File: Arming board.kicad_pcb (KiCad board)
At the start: 4 copper layers, 22 parts, among them IC1 CD4043BDR, J3 Conn_01x04, Q1 SQS141ELNW-T1_GE3

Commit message: Basic routing and fixes
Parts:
- added H1: MountingHole_Pad, MountingHole:MountingHole_3.2mm_M3_DIN965_Pad_TopBottom, F.Cu at (99.5, 112.5)
- added H2: MountingHole_Pad, MountingHole:MountingHole_3.2mm_M3_DIN965_Pad_TopBottom, F.Cu at (66.5, 112.5)
- added H3: MountingHole_Pad, MountingHole:MountingHole_3.2mm_M3_DIN965_Pad_TopBottom, F.Cu at (100.0, 75.5)
- added H4: MountingHole_Pad, MountingHole:MountingHole_3.2mm_M3_DIN965_Pad_TopBottom, F.Cu at (67.0, 75.0)
- C1, C2: value 1u -> 10u
- R3, R4: value 10k -> 1k
- R6, R7: value 10k -> 80k
- moved D6 54.7 mm to (72.5, 79.4), turned to 180 degrees
- moved D19 43.5 mm to (94.6, 79.4)
- moved Q1 42.2 mm to (82.5, 80.6)
- moved J4 33.8 mm to (71.3, 99.5), turned to 90 degrees
- moved R7 31.0 mm to (83.8, 99.7)
- moved IC1 30.2 mm to (83.6, 91.8), turned to 90 degrees
- moved J2 28.0 mm to (96.0, 84.9), turned to -90 degrees
- moved R6 28.0 mm to (87.0, 99.1), turned to 180 degrees
- moved R1 27.2 mm to (79.9, 84.5), turned to 180 degrees
- moved J5 25.3 mm to (96.0, 97.6), turned to -90 degrees
- moved R2 21.7 mm to (87.0, 84.5), turned to 180 degrees
- moved C1 20.8 mm to (87.0, 101.0)
- moved C2 19.3 mm to (83.7, 101.0), turned to 180 degrees
- moved D1 18.7 mm to (84.5, 104.2), turned to 90 degrees
- moved J1 16.7 mm to (71.4, 87.5), turned to 90 degrees
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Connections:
- D5 pad 1: +BATT -> VCC
- D6 pad 1: +BATT -> VCC
- IC1 pad 11: unconnected-(IC1-R3-Pad11) -> GND
- IC1 pad 12: unconnected-(IC1-S3-Pad12) -> GND
- IC1 pad 14: unconnected-(IC1-S4-Pad14) -> GND
- IC1 pad 15: unconnected-(IC1-R4-Pad15) -> GND
- IC1 pad 3: unconnected-(IC1-R1-Pad3) -> GND
- IC1 pad 4: unconnected-(IC1-S1-Pad4) -> GND
- J1 pad 3: +BATT -> VCC
- J1 pad 4: +BATT -> VCC
- J3 pad 2: Net-(D3-K) -> Net-(D1-K)
- J3 pad 3: Net-(D1-K) -> Net-(D3-K)
- J4 pad 3: +BATT -> VCC
- J4 pad 4: +BATT -> VCC
- Q1 pad 1: +BATT -> VCC
- Q1 pad 2: +BATT -> VCC
- Q1 pad 3: +BATT -> VCC
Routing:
- net VCC: track 0.00 -> 12.5 mm
- net disarm: track 0.00 -> 9.11 mm
- net Net-(Q1-Pad4): track 0.00 -> 8.18 mm
- net arm: track 0.00 -> 7.30 mm
- net Net-(IC1-ENABLE): track 0.00 -> 5.14 mm
- net Net-(D3-K): track 0.00 -> 4.60 mm
- net Net-(D1-K): track 0.00 -> 4.49 mm
- net Net-(IC1-Q2): track 0.00 -> 2.93 mm
- net GND: vias 0 -> 15
- added copper zone on F.Cu, net +BATT_ARM
- added copper zone on B.Cu, net GND
- added copper zone on F.Cu, net GND
- added copper zone on F.Cu, net VCC
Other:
- board outline added: 43.5 x 46.3 mm
- copper layers 4 -> 2
- board text added: "Arming Board"
- board text added: "JLCJLCJLCJLC"
- board text added: "rev1"

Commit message: improve routing
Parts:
- added G***: LOGO, frodo_io_module:rapid_logo, B.Cu at (129.6, 122.8)
- added TP1: TestPoint, TestPoint:TestPoint_Pad_D1.0mm, F.Cu at (140.5, 125.0)
- added TP2: TestPoint, TestPoint:TestPoint_Pad_D1.0mm, B.Cu at (137.5, 146.0)
- added TP3: TestPoint, TestPoint:TestPoint_Pad_D1.0mm, B.Cu at (134.5, 146.0)
- added TP4: TestPoint, TestPoint:TestPoint_Pad_D1.0mm, F.Cu at (127.5, 119.7)
- added TP5: TestPoint, TestPoint:TestPoint_Pad_D1.0mm, F.Cu at (144.8, 120.4)
- moved H3 94.7 mm to (153.0, 154.0)
- moved H4 94.6 mm to (119.0, 154.0)
- moved D6 70.1 mm to (125.7, 125.0)
- moved J1 69.8 mm to (124.4, 132.8)
- moved J4 69.5 mm to (124.4, 144.2)
- moved D5 68.8 mm to (130.3, 143.8), turned to 0 degrees
- moved D19 68.7 mm to (146.3, 124.6)
- moved J2 68.3 mm to (147.6, 129.7)
- moved D3 67.6 mm to (133.2, 145.1)
- moved J5 67.6 mm to (147.6, 141.2)
- moved J3 67.3 mm to (140.5, 148.6)
- moved Q1 67.3 mm to (136.0, 121.6)
- moved R4 67.2 mm to (134.5, 145.2)
- moved D1 67.0 mm to (137.8, 144.8)
- moved IC1 67.0 mm to (136.0, 133.4)
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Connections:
- D1 pad 1: Net-(D1-K) -> arm
- D3 pad 1: Net-(D3-K) -> disarm
- J3 pad 2: Net-(D1-K) -> arm
- J3 pad 3: Net-(D3-K) -> disarm
- R3 pad 2: Net-(D1-K) -> arm
- R4 pad 2: Net-(D3-K) -> disarm
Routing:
- net VCC: track 12.5 -> 21.3 mm
- net disarm: track 9.11 -> 17.8 mm
- net arm: track 7.30 -> 15.5 mm
- net GND: track 0.00 -> 7.27 mm, vias 15 -> 283
- net Net-(D3-K): track 4.60 -> 0.00 mm
- net Net-(D1-K): track 4.49 -> 0.00 mm
- net +BATT_ARM: track 0.00 -> 3.21 mm
- net Net-(IC1-Q2): track 2.93 -> 5.58 mm
- net Net-(IC1-ENABLE): track 5.14 -> 6.14 mm
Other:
- board size 43.5 x 46.3 mm -> 42 x 42 mm
- board text added: "ARM"
- board text added: "ARMED"
- board text added: "DISARM"
- board text added: "GND"
- board text added: "Power In"
- board text added: "Power Out"
- board text added: "Q"
- board text added: "VCC"

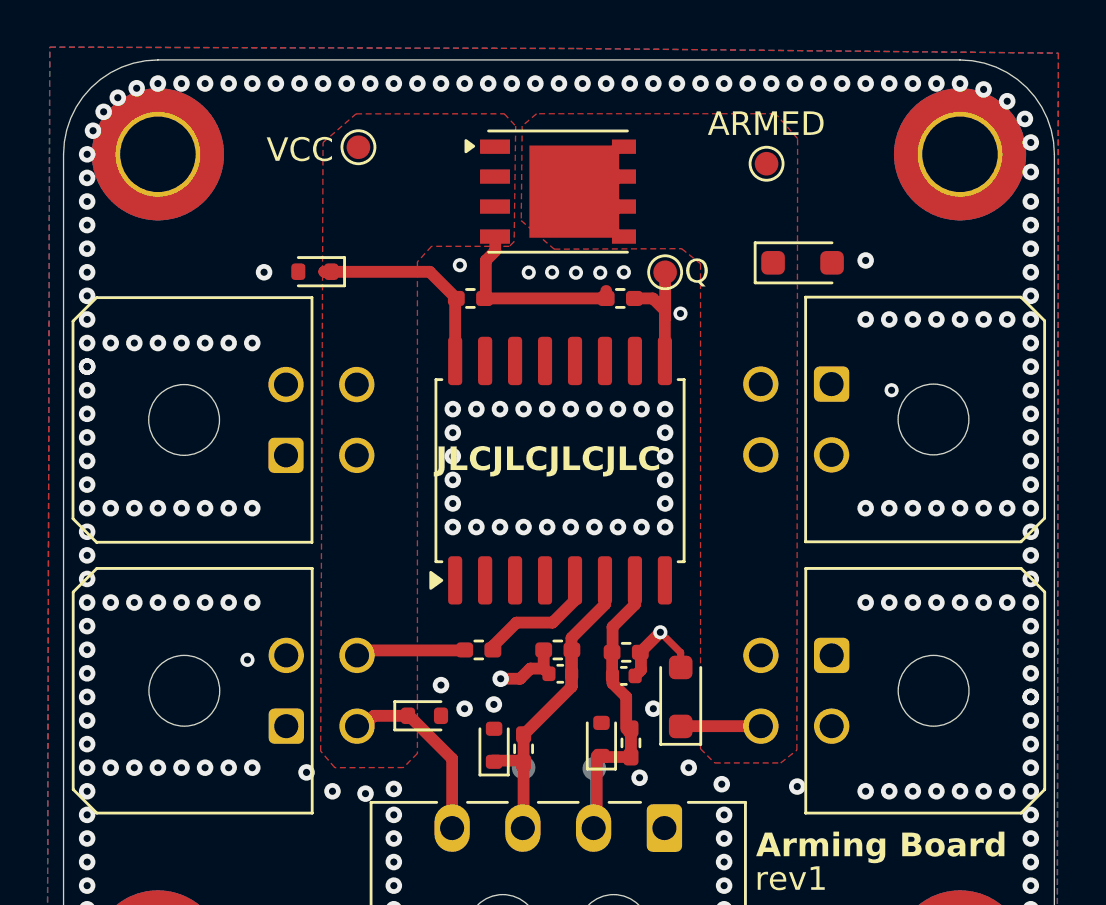
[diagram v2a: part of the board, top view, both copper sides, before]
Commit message: check parts, replace mosfet
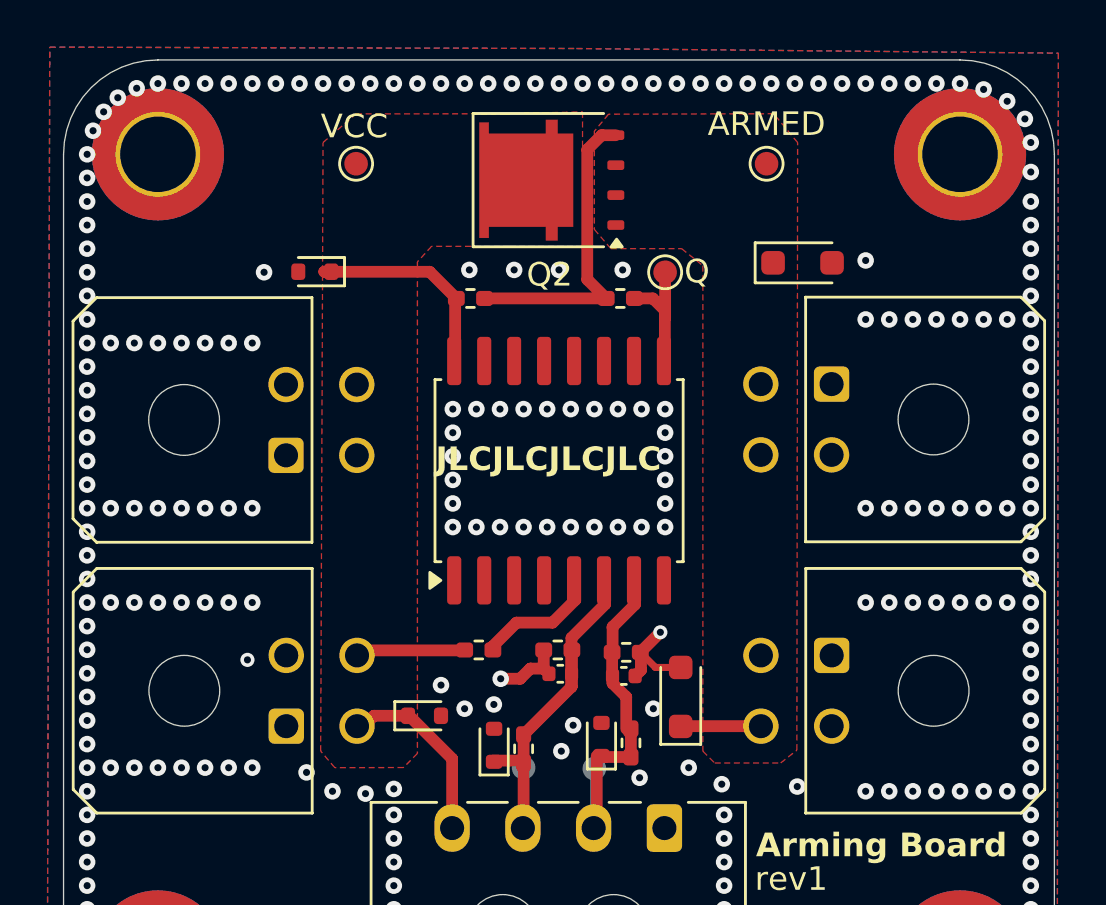
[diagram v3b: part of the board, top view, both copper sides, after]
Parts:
- removed Q1: SQS141ELNW-T1_GE3, Package_SO:PowerPAK_SO-8_Single
- added Q2: SQJ409EP, Package_SO:PowerPAK_SO-8L_Single, F.Cu at (135.7, 121.1)
- R1, R5: value 10k -> 12k
- R6, R7: value 80k -> 51k
- moved TP4 0.71 mm to (127.4, 120.4)
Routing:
- net Net-(Q2-G): track 8.30 -> 13.3 mm
- net GND: track 7.27 -> 7.40 mm, vias 283 -> 279

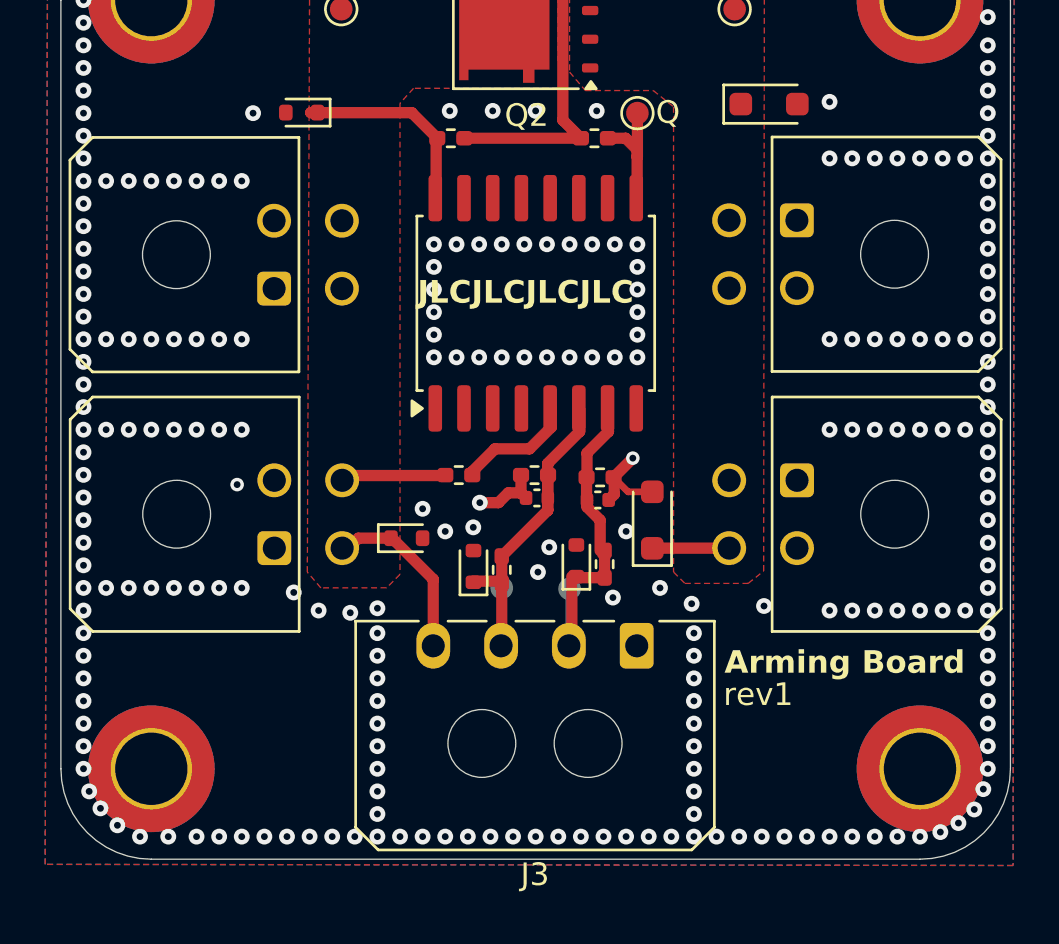
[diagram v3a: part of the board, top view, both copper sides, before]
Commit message: improve silkscreen
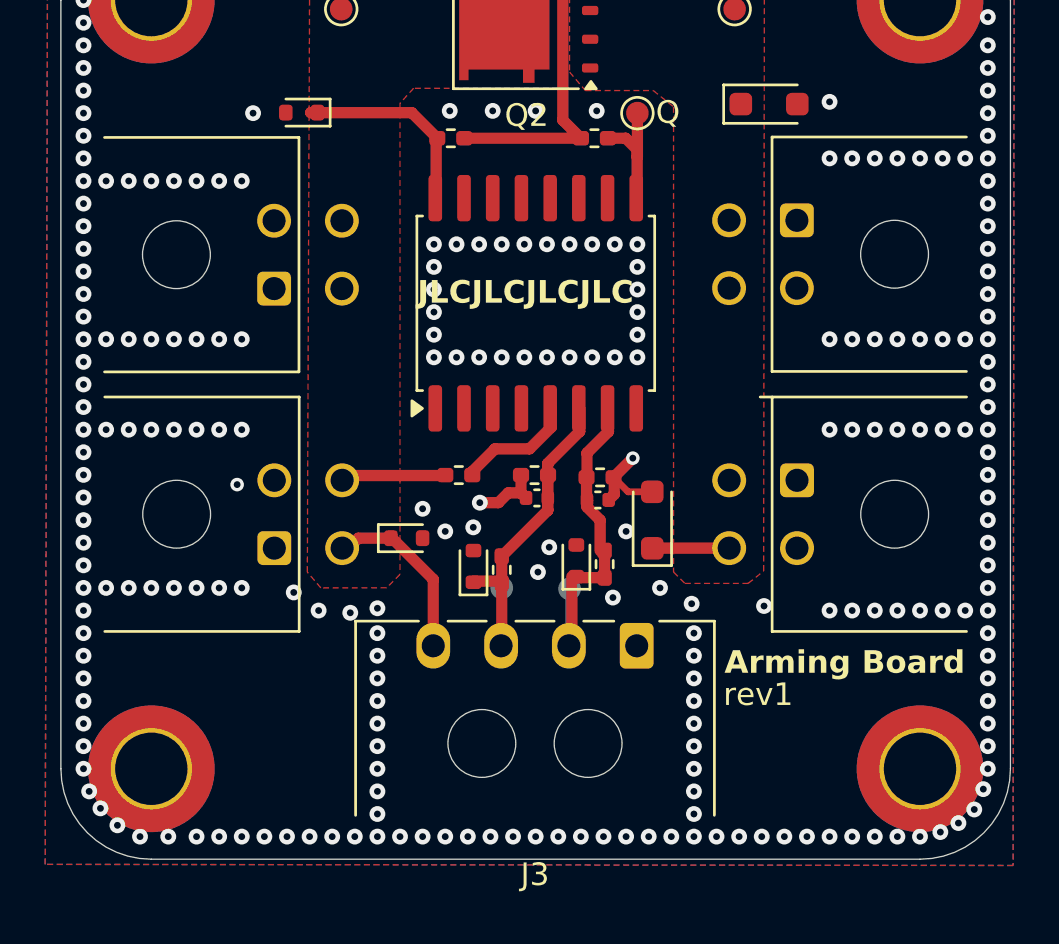
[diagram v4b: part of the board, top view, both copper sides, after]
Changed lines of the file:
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@@
 		(sheetname "/")
 		(sheetfile "Arming board.kicad_sch")
-		(units
-			(unit
-				(name "A")
-				(pins "1" "2" "3" "4")
-			)
-		)
 		(attr through_hole dnp)
 		(duplicate_pad_numbers_are_jumpers no)
 		(fp_line
-			(start 5.685 -9.03)
-			(end 6.685 -8.03)
-			(stroke
-				(width 0.12)
-				(type solid)
-			)
-			(layer "F.SilkS")
-		)
-		(fp_line
-			(start -2.685 -9.03)
-			(end 5.685 -9.03)
-			(stroke
-				(width 0.12)
-				(type solid)
-			)
-			(layer "F.SilkS")
-		)
-		(fp_line
-			(start 6.685 -8.03)
+			(start 6.685 -7.5)
 			(end 6.685 1.1)
 			(stroke
@@
 		)
 		(fp_line
-			(start -3.685 -8.03)
-			(end -2.685 -9.03)
-			(stroke
-				(width 0.12)
-				(type solid)
-			)
-			(layer "F.SilkS")
-		)
-		(fp_line
 			(start 6.685 1.1)
 			(end -3.685 1.1)
@@
 		(fp_line
 			(start -3.685 1.1)
-			(end -3.685 -8.03)
+			(end -3.685 -7.5)
 			(stroke
 				(width 0.12)
@@
 		(sheetname "/")
 		(sheetfile "Arming board.kicad_sch")
-		(units
-			(unit
-				(name "A")
-				(pins "1" "2" "3" "4")
-			)
-		)
 		(attr through_hole dnp)
 		(duplicate_pad_numbers_are_jumpers no)
 		(fp_line
 			(start -3.685 1.1)
-			(end -3.685 -8.03)
+			(end -3.685 -7.5)
 			(stroke
 				(width 0.12)
@@
 		)
 		(fp_line
-			(start -3.685 -8.03)
-			(end -2.685 -9.03)
-			(stroke
-				(width 0.12)
-				(type solid)
-			)
-			(layer "F.SilkS")
-		)
-		(fp_line
-			(start 6.685 -8.03)
+			(start 6.685 -7.5)
 			(end 6.685 1.1)
 			(stroke
@@
 		)
 		(fp_line
-			(start -2.685 -9.03)
-			(end 5.685 -9.03)
-			(stroke
-				(width 0.12)
-				(type solid)
-			)
-			(layer "F.SilkS")
-		)
-		(fp_line
-			(start 5.685 -9.03)
-			(end 6.685 -8.03)
-			(stroke
-				(width 0.12)
-				(type solid)
-			)
-			(layer "F.SilkS")
-		)
-		(fp_line
 			(start -1.25 4.25)
 			(end -1.25 1.49)
@@
 		(sheetname "/")
 		(sheetfile "Arming board.kicad_sch")
-		(units
-			(unit
-				(name "A")
-				(pins "1" "2" "3" "4")
-			)
-		)
 		(attr through_hole dnp)
 		(duplicate_pad_numbers_are_jumpers no)
 		(fp_line
-			(start -3.685 1.1)
-			(end -3.685 -8.03)
+			(start -3.685 1.63)
+			(end -3.685 -7.5)
 			(stroke
 				(width 0.12)
@@
 		)
 		(fp_line
-			(start -3.685 -8.03)
-			(end -2.685 -9.03)
-			(stroke
-				(width 0.12)
-				(type solid)
-			)
-			(layer "F.SilkS")
-		)
-		(fp_line
-			(start 6.685 -8.03)
+			(start 6.685 -7.5)
 			(end 6.685 1.1)
 			(stroke
@@
 		)
 		(fp_line
-			(start -2.685 -9.03)
-			(end 5.685 -9.03)
-			(stroke
-				(width 0.12)
-				(type solid)
-			)
-			(layer "F.SilkS")
-		)
-		(fp_line
-			(start 5.685 -9.03)
-			(end 6.685 -8.03)
-			(stroke
-				(width 0.12)
-				(type solid)
-			)
-			(layer "F.SilkS")
-		)
-		(fp_line
 			(start -1.25 4.25)
 			(end -1.25 1.5)
@@
 		(sheetname "/")
 		(sheetfile "Arming board.kicad_sch")
-		(units
-			(unit
-				(name "A")
-				(pins "1" "2" "3" "4")
-			)
-		)
 		(attr through_hole dnp)
 		(duplicate_pad_numbers_are_jumpers no)
 		(fp_line
-			(start 5.685 -9.03)
-			(end 6.685 -8.03)
-			(stroke
-				(width 0.12)
-				(type solid)
-			)
-			(layer "F.SilkS")
-		)
-		(fp_line
-			(start -2.685 -9.03)
-			(end 5.685 -9.03)
-			(stroke
-				(width 0.12)
-				(type solid)
-			)
-			(layer "F.SilkS")
-		)
-		(fp_line
-			(start 6.685 -8.03)
+			(start 6.685 -7.5)
 			(end 6.685 1.1)
 			(stroke
@@
 		)
 		(fp_line
-			(start -3.685 -8.03)
-			(end -2.685 -9.03)
-			(stroke
-				(width 0.12)
-				(type solid)
-			)
-			(layer "F.SilkS")
-		)
-		(fp_line
 			(start 6.685 1.1)
 			(end -3.685 1.1)
@@
 		(fp_line
 			(start -3.685 1.1)
-			(end -3.685 -8.03)
+			(end -3.685 -7.5)
 			(stroke
 				(width 0.12)
@@
 		)
 		(fp_text user "${REFERENCE}"
-			(at 1.5 -8.22 90)
+			(at 0 -11.5 90)
 			(layer "F.Fab")
 			(effects
@@
 		(sheetname "/")
 		(sheetfile "Arming board.kicad_sch")
-		(units
-			(unit
-				(name "A")
-				(pins "1" "2" "3" "4")
-			)
-		)
 		(attr through_hole dnp)
 		(duplicate_pad_numbers_are_jumpers no)
@@
 		)
 		(fp_line
-			(start 12.435 -8.03)
+			(start 12.435 -7.5)
 			(end 12.435 1.09)
 			(stroke
@@
 		)
 		(fp_line
-			(start 11.435 -9.03)
-			(end 12.435 -8.03)
-			(stroke
-				(width 0.12)
-				(type solid)
-			)
-			(layer "F.SilkS")
-		)
-		(fp_line
 			(start 6.651767 1.09)
 			(end 8.348233 1.09)
@@
 		)
 		(fp_line
-			(start -2.435 -9.03)
-			(end 11.435 -9.03)
-			(stroke
-				(width 0.12)
-				(type solid)
-			)
-			(layer "F.SilkS")
-		)
-		(fp_line
 			(start -3.435 1.09)
 			(end -1.01 1.09)
@@
 		(fp_line
 			(start -3.435 1.09)
-			(end -3.435 -8.03)
-			(stroke
-				(width 0.12)
-				(type solid)
-			)
-			(layer "F.SilkS")
-		)
-		(fp_line
-			(start -3.435 -8.03)
-			(end -2.435 -9.03)
+			(end -3.435 -7.5)
 			(stroke
 				(width 0.12)

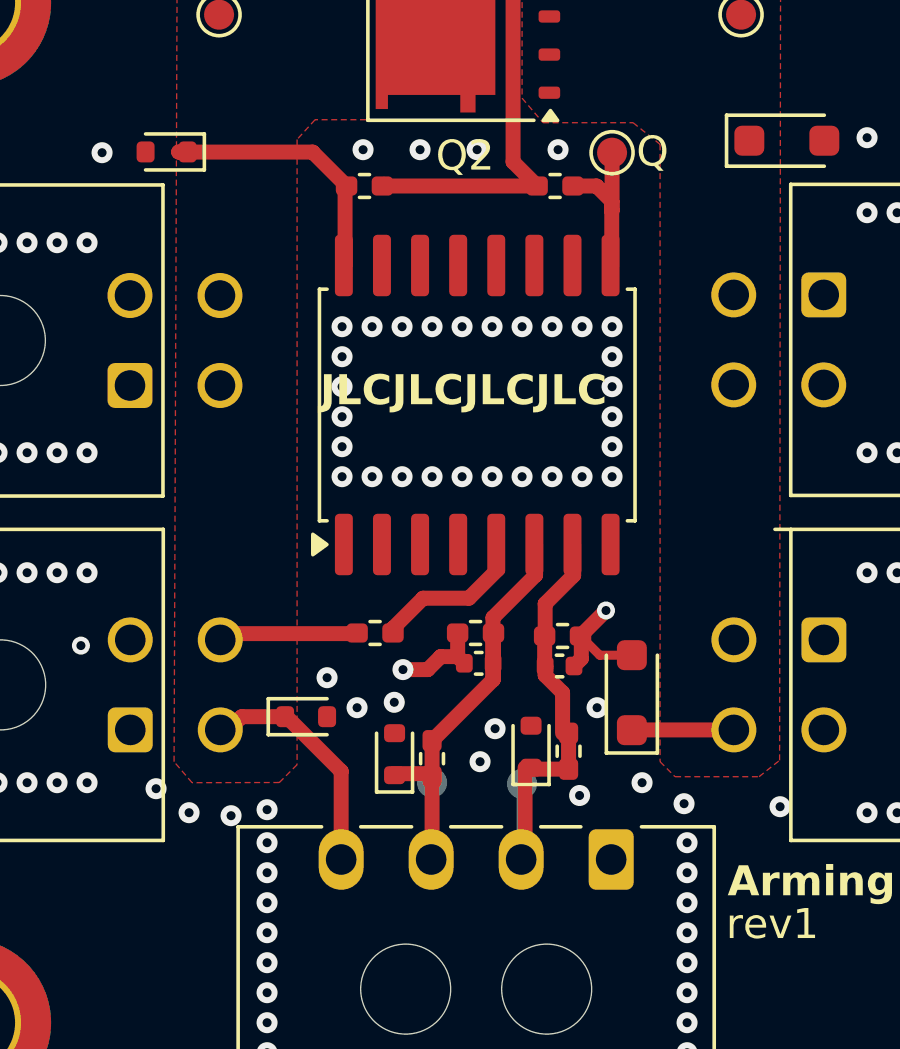
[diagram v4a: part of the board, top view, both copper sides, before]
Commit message: change flipflop footprint
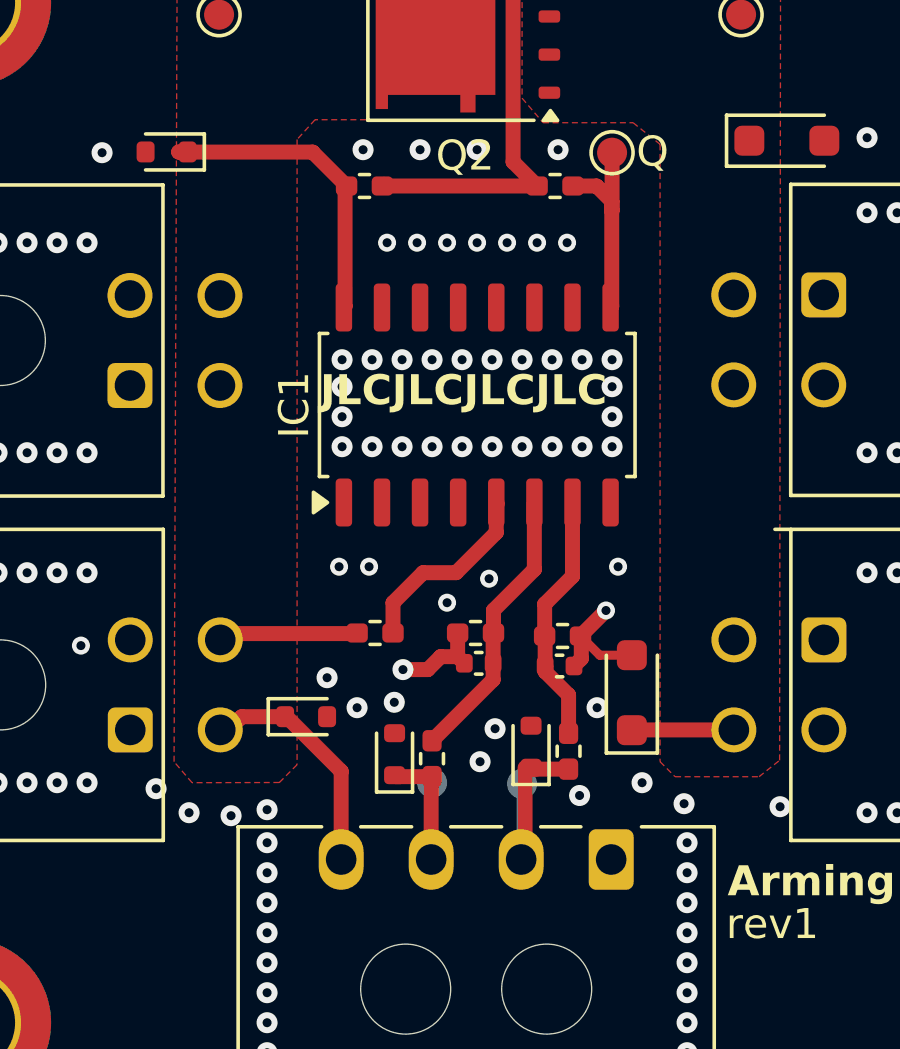
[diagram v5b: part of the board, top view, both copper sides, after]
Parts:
- IC1: footprint Package_SO:SOIC-16W_7.5x10.3mm_P1.27mm -> Package_SO:SOIC-16_4.55x10.3mm_P1.27mm
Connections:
- C1 pad 1: arm -> arm_signal
- C2 pad 1: disarm -> disarm_signal
- D1 pad 1: arm -> /arm
- D3 pad 1: disarm -> /disarm
- IC1 pad 6: disarm -> disarm_signal
- IC1 pad 7: arm -> arm_signal
- J3 pad 2: arm -> /arm
- J3 pad 3: disarm -> /disarm
- R3 pad 1: arm -> arm_signal
- R3 pad 2: arm -> /arm
- R4 pad 1: disarm -> disarm_signal
- R4 pad 2: disarm -> /disarm
- R6 pad 2: arm -> arm_signal
- R7 pad 2: disarm -> disarm_signal
- TP2 pad 1: arm -> /arm
- TP3 pad 1: disarm -> /disarm
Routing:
- net disarm: track 17.8 -> 0.00 mm
- net arm: track 15.5 -> 0.00 mm
- net disarm_signal: track 0.00 -> 9.35 mm
- net arm_signal: track 0.00 -> 8.47 mm
- net /arm: track 0.00 -> 7.29 mm
- net /disarm: track 0.00 -> 6.62 mm
- net Net-(IC1-Q2): track 5.58 -> 7.00 mm
- net VCC: track 21.3 -> 22.5 mm
- net GND: vias 279 -> 287
